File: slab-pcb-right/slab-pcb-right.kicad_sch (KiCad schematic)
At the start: 125 parts, among them J1 MagnetR, J2 MagnetL, J3 TRRS_R, J4 TRRS_L, J5 SSD1306, J6 Conn_01x06, Q1 MMBT3906, SW1 RotaryEncoder, U1 Seeeduino Xiao rp2040, U2 PCA9555PW, U3 PCA9555PW, U4 ADS1110, U5 SN74AHCT125PWR

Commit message: fix: inconsistent design
all modules now share the same design - with updated footprints to
support both choc+mx PCB mounting holes.
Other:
- company: (none) -> Edward Hesketh
- title: (none) -> The Slab Keyboard - Right Module
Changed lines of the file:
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@@
 	(generator_version "8.0")
 	(paper "A4")
+	(title_block
+		(title "The Slab Keyboard - Right Module")
+		(date "2024-10-16")
+		(company "Edward Hesketh")
+	)
 	(junction
 		(at 227.33 148.59)

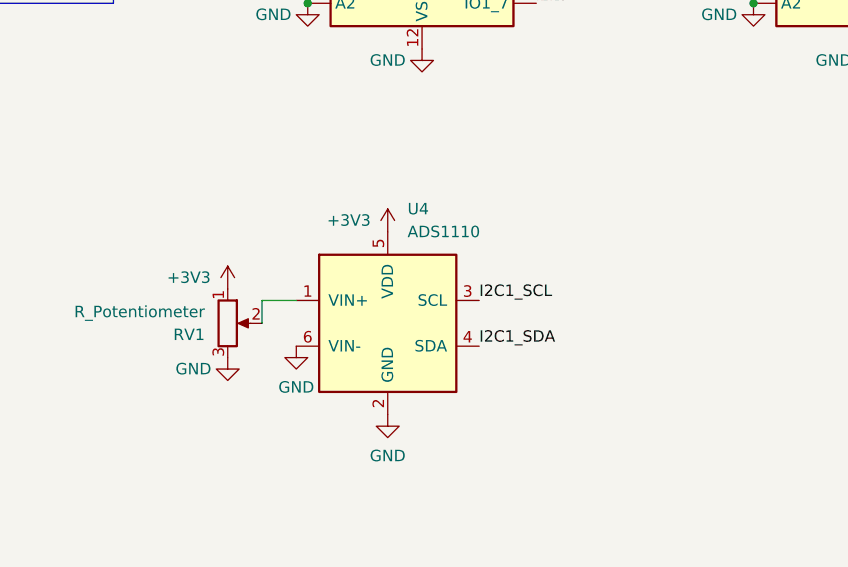
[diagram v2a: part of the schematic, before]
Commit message: fix: add voltage divider to potentiometer
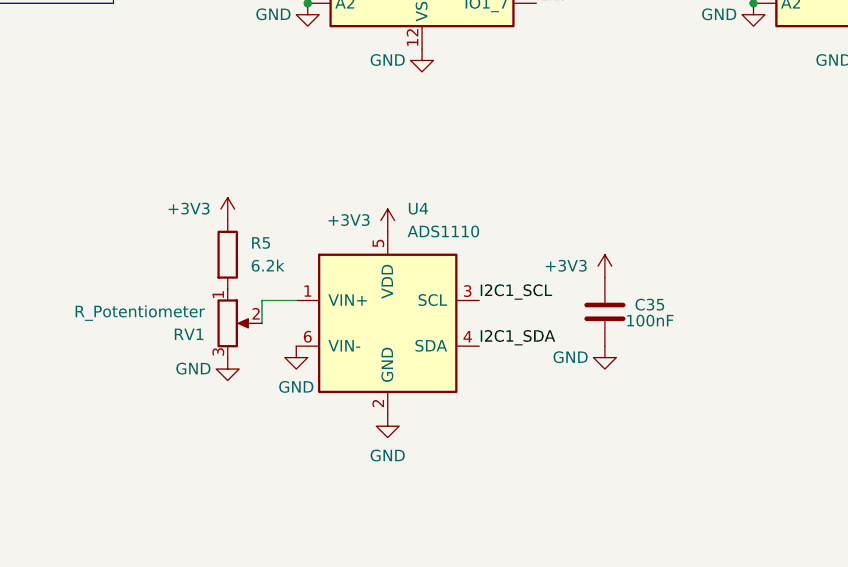
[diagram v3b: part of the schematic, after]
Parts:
- added C35: 100nF, Capacitor_SMD:C_0603_1608Metric_Pad1.08x0.95mm_HandSolder, symbol Device:C
- added R5: 6.2k, Resistor_SMD:R_0603_1608Metric_Pad0.98x0.95mm_HandSolder, symbol Device:R
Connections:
- net +3V3: now also C35.2, R5.1; no longer RV1.1
- net GND: now also C35.1
- new net: R5.2, RV1.1

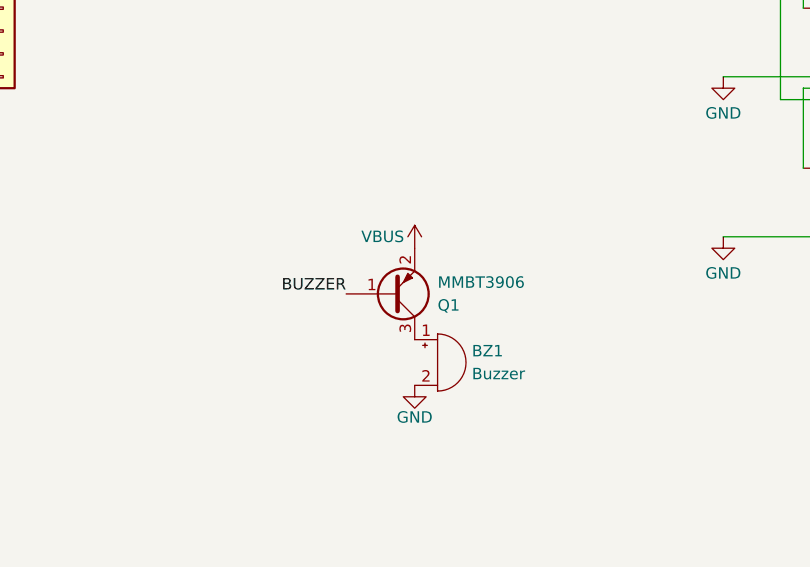
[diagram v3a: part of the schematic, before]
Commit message: feat: use slots instead of overlapped drill hits
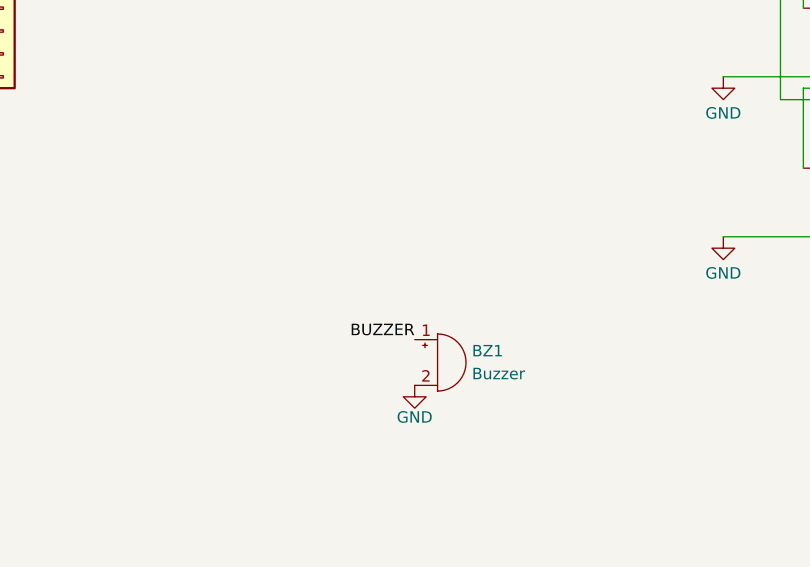
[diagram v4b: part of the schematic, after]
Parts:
- removed Q1: MMBT3906, Package_TO_SOT_SMD:SOT-23, symbol Transistor_BJT:MMBT3906
- BZ1: footprint Buzzer_Beeper:MagneticBuzzer_CUI_CMT-8504-100-SMT -> CustomFootprints:buzzer
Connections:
- net BUZZER: now also BZ1.1 (+)
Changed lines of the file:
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@@
 	)
 	(label "BUZZER"
-		(at 138.43 172.72 180)
+		(at 146.05 177.8 180)
 		(fields_autoplaced yes)
 		(effects
@@
 	)
 	(symbol
-		(lib_id "power:VBUS")
-		(at 146.05 167.64 0)
-		(unit 1)
-		(exclude_from_sim no)
-		(in_bom yes)
-		(on_board yes)
-		(dnp no)
-		(property "Reference" "#PWR039"
-			(at 146.05 171.45 0)
-			(effects
-				(font
-					(size 1.27 1.27)
-				)
-				(hide yes)
-			)
-		)
-		(property "Value" "VBUS"
-			(at 142.494 166.37 0)
-			(effects
-				(font
-					(size 1.27 1.27)
-				)
-			)
-		)
-		(property "Footprint" ""
-			(at 146.05 167.64 0)
-			(effects
-				(font
-					(size 1.27 1.27)
-				)
-				(hide yes)
-			)
-		)
-		(property "Datasheet" ""
-			(at 146.05 167.64 0)
-			(effects
-				(font
-					(size 1.27 1.27)
-				)
-				(hide yes)
-			)
-		)
-		(property "Description" "Power symbol creates a global label with name \"VBUS\""
-			(at 146.05 167.64 0)
-			(effects
-				(font
-					(size 1.27 1.27)
-				)
-				(hide yes)
-			)
-		)
-		(pin "1"
-		)
-		(instances
-			(project "slab-pcb-right"
-				(path "/2d36872c-cd86-4c0b-a812-2eca2fd821a3"
-					(reference "#PWR039")
-					(unit 1)
-				)
-			)
-		)
-	)
-	(symbol
 		(lib_id "Connector_Generic:Conn_01x04")
 		(at 55.88 133.35 180)
@@
 	)
 	(symbol
-		(lib_id "Transistor_BJT:MMBT3906")
-		(at 143.51 172.72 0)
-		(mirror x)
-		(unit 1)
-		(exclude_from_sim no)
-		(in_bom yes)
-		(on_board yes)
-		(dnp no)
-		(property "Reference" "Q1"
-			(at 148.59 173.9901 0)
-			(effects
-				(font
-					(size 1.27 1.27)
-				)
-				(justify left)
-			)
-		)
-		(property "Value" "MMBT3906"
-			(at 148.59 171.4501 0)
-			(effects
-				(font
-					(size 1.27 1.27)
-				)
-				(justify left)
-			)
-		)
-		(property "Footprint" "Package_TO_SOT_SMD:SOT-23"
-			(at 148.59 170.815 0)
-			(effects
-				(font
-					(size 1.27 1.27)
-					(italic yes)
-				)
-				(justify left)
-				(hide yes)
-			)
-		)
-		(property "Datasheet" "https://www.onsemi.com/pdf/datasheet/pzt3906-d.pdf"
-			(at 143.51 172.72 0)
-			(effects
-				(font
-					(size 1.27 1.27)
-				)
-				(justify left)
-				(hide yes)
-			)
-		)
-		(property "Description" "-0.2A Ic, -40V Vce, Small Signal PNP Transistor, SOT-23"
-			(at 143.51 172.72 0)
-			(effects
-				(font
-					(size 1.27 1.27)
-				)
-				(hide yes)
-			)
-		)
-		(pin "1"
-		)
-		(pin "3"
-		)
-		(pin "2"
-		)
-		(instances
-			(project "slab-pcb-right"
-				(path "/2d36872c-cd86-4c0b-a812-2eca2fd821a3"
-					(reference "Q1")
-					(unit 1)
-				)
-			)
-		)
-	)
-	(symbol
 		(lib_id "power:GND")
 		(at 180.34 113.03 0)
@@
 			)
 		)
-		(property "Footprint" "Buzzer_Beeper:MagneticBuzzer_CUI_CMT-8504-100-SMT"
+		(property "Footprint" "CustomFootprints:buzzer"
 			(at 147.955 177.8 90)
 			(effects

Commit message: feat: start on v4, updated: right-hand schematic
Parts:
- removed C1, C10, C11, C12, C13, C14, C15, C16, C17, C18, C19, C2, C20, C21, C22, C23, C24, C25, C26, C27, C28, C29, C3, C30, C4, C5, C6, C7, C8, C9: 100nF, Capacitor_SMD:C_0603_1608Metric_Pad1.08x0.95mm_HandSolder, symbol Device:C
- removed J6: Conn_01x06, Connector_PinHeader_2.54mm:PinHeader_1x06_P2.54mm_Vertical, symbol Connector_Generic:Conn_01x06
- removed LED1, LED10, LED11, LED12, LED13, LED14, LED15, LED16, LED17, LED18, LED19, LED2, LED20, LED21, LED22, LED23, LED24, LED25, LED26, LED27, LED28, LED29, LED3, LED30, LED4, LED5, LED6, LED7, LED8, LED9: MX_SK6812MINI-E, CustomFootprints:LED_MX_6028R-ROT_Custom, symbol PCM_marbastlib-mx:MX_SK6812MINI-E
- removed TP1: NPIXEL_SHIFT, TestPoint:TestPoint_Pad_1.0x1.0mm, symbol Connector:TestPoint
- removed TP2: NPIXEL_IN, TestPoint:TestPoint_Pad_1.0x1.0mm, symbol Connector:TestPoint
- added C36: 100nF, Capacitor_SMD:C_0603_1608Metric_Pad1.08x0.95mm_HandSolder, symbol Device:C
- added R10, R7, R8, R9: 2.2k, Resistor_SMD:R_0603_1608Metric_Pad0.98x0.95mm_HandSolder, symbol Device:R
- added R6: 10k, Resistor_SMD:R_0603_1608Metric_Pad0.98x0.95mm_HandSolder, symbol Device:R
- added U6: TCA4307DGKR, SOIC8_DGK_TEX, symbol CustomSymbols:TCA4307DGKR
- J1: value MagnetR -> Conn_01x04; footprint CustomFootprints:5358_mag_connector_1x4_pads -> (none)
- J2: value MagnetL -> Conn_01x04; footprint CustomFootprints:5358_mag_connector_1x4_pins -> (none)
- RV1: value R_Potentiometer -> Slider
- renumbered J4 to J3, J3 to J4
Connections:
- net UART0_RX is gone; now on net SHIFTER_INPUT: U1.14 (P1)
- net +3V3: now also C32.2, C33.2, C34.2, U5.14 (VCC), C36.2, R10.2, R6.1, R7.1, R8.1, R9.2, U6.1 (EN), U6.8 (VCC); no longer C32.1, C33.1
- net BUZZER: now also U1.11 (P3); no longer U1.13 (P2)
- net EXPANDER1_INT: now also U1.13 (P2); no longer U3.13 (IO1_0)
- net EXPANDER2_INT: now also U1.12 (P4); no longer U1.11 (P3)
- net GND: now also C32.1, C33.1, J1.3 (Pin_3), J2.3 (Pin_3), C36.1, U6.4 (GND); no longer C32.2, C33.2, J1.1 (Pin_1), J2.1 (Pin_1)
- net I2C0_SCL: now also J5.3 (Pin_3), R1.2, U2.22 (SCL), U3.22 (SCL), U4.3 (SCL); no longer J1.2 (Pin_2), J4.R1
- net I2C0_SDA: now also J5.4 (Pin_4), R2.2, U2.23 (SDA), U3.23 (SDA), U4.4 (SDA); no longer J1.3 (Pin_3), J4.R2
- net I2C1_SCL: now also R7.2, U6.2 (SCLOUT); no longer J2.2 (Pin_2), J3.R1, J5.3 (Pin_3), R2.2, U2.22 (SCL), U3.22 (SCL), U4.3 (SCL)
- net I2C1_SDA: now also R8.2, U6.7 (SDAOUT); no longer J2.3 (Pin_3), J3.R2, J5.4 (Pin_4), R1.2, U2.23 (SDA), U3.23 (SDA), U4.4 (SDA)
- net VBUS: no longer C34.2, U5.14 (VCC)
- net RGB LED Array/Output: now reaches LED31.3 (DIN)
- net ENCODER_A renamed ROT_A
- net ENCODER_B renamed ROT_B
- net KEY_PIXEL_INPUT renamed SHIFTER_OUTPUT
- net KEY_PIXEL_SHIFT_INPUT renamed SHIFTER_INPUT
- net SHIFTER_INPUT: no longer U1.12 (P4)
- net UART0_TX renamed I2C1_RDY
- net I2C1_RDY: now also R6.2, U6.5 (READY)
- new net I2C_BUS_SCL: J1.2 (Pin_2), J2.2 (Pin_2), J3.R2, J4.R2, R9.1, U6.3 (SCLIN)
- new net I2C_BUS_SDA: J1.1 (Pin_1), J2.1 (Pin_1), J3.R1, J4.R1, R10.1, U6.6 (SDAIN)
- no-connect marks 19 -> 18
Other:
- added sheet RGB LED Array (RGBLEDArray.kicad_sch)
- note added: "ADC and slider/potentiometer"
- note added: "Buzzer"
- note added: "I2C0 (to onboard peripherals)"
- note added: "I2C0 pullup resistors"
- note added: "I2C1 (to other keyboards)"
- note added: "Key switch array"
- note added: "Logic level changer and main LED array"
- note added: "OLED screen"
- note added: "Rotary encoder with LED"
- note removed: "Seeeduino Xiao RP2040"
- title: The Slab Keyboard - Right Module -> The Interchange Keyboard - Right Module
- moved on the sheet: BZ1, C32, H1, H2, H3, H4, H5, H6, H7, H8, H9, J3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

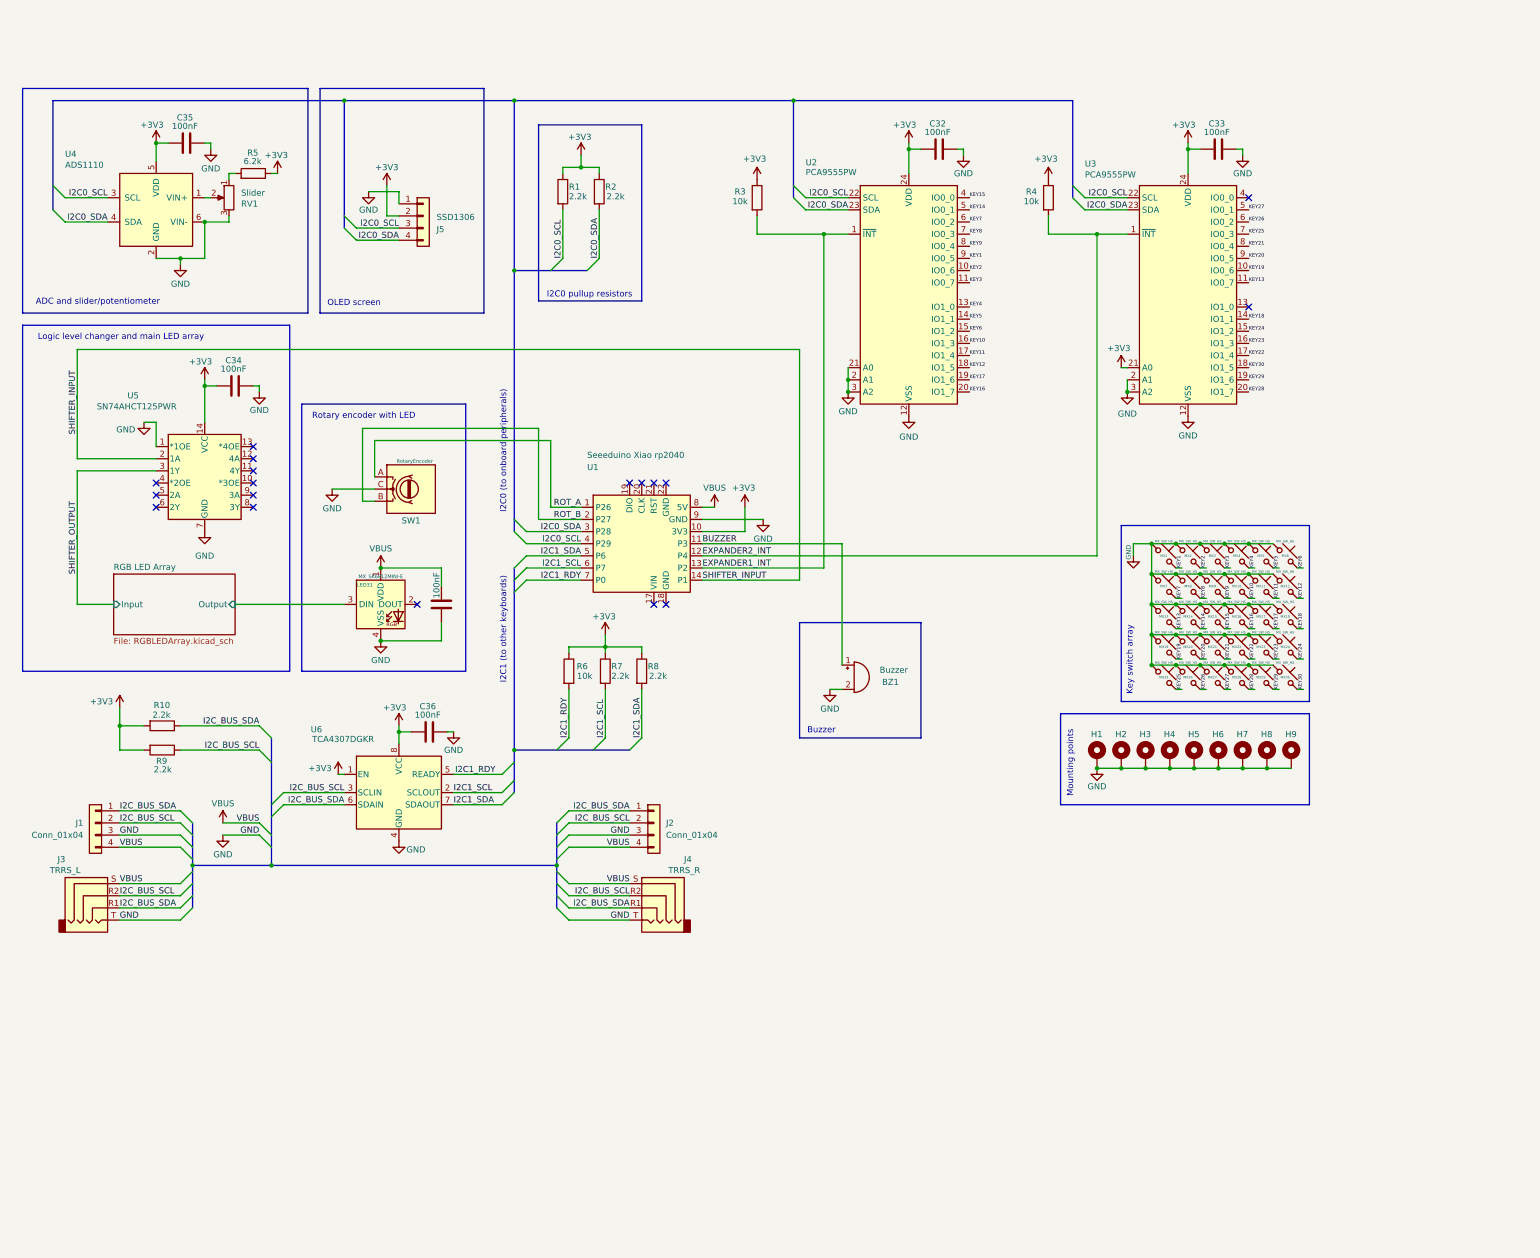
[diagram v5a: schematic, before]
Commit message: feat: route most of slab-pcb-right
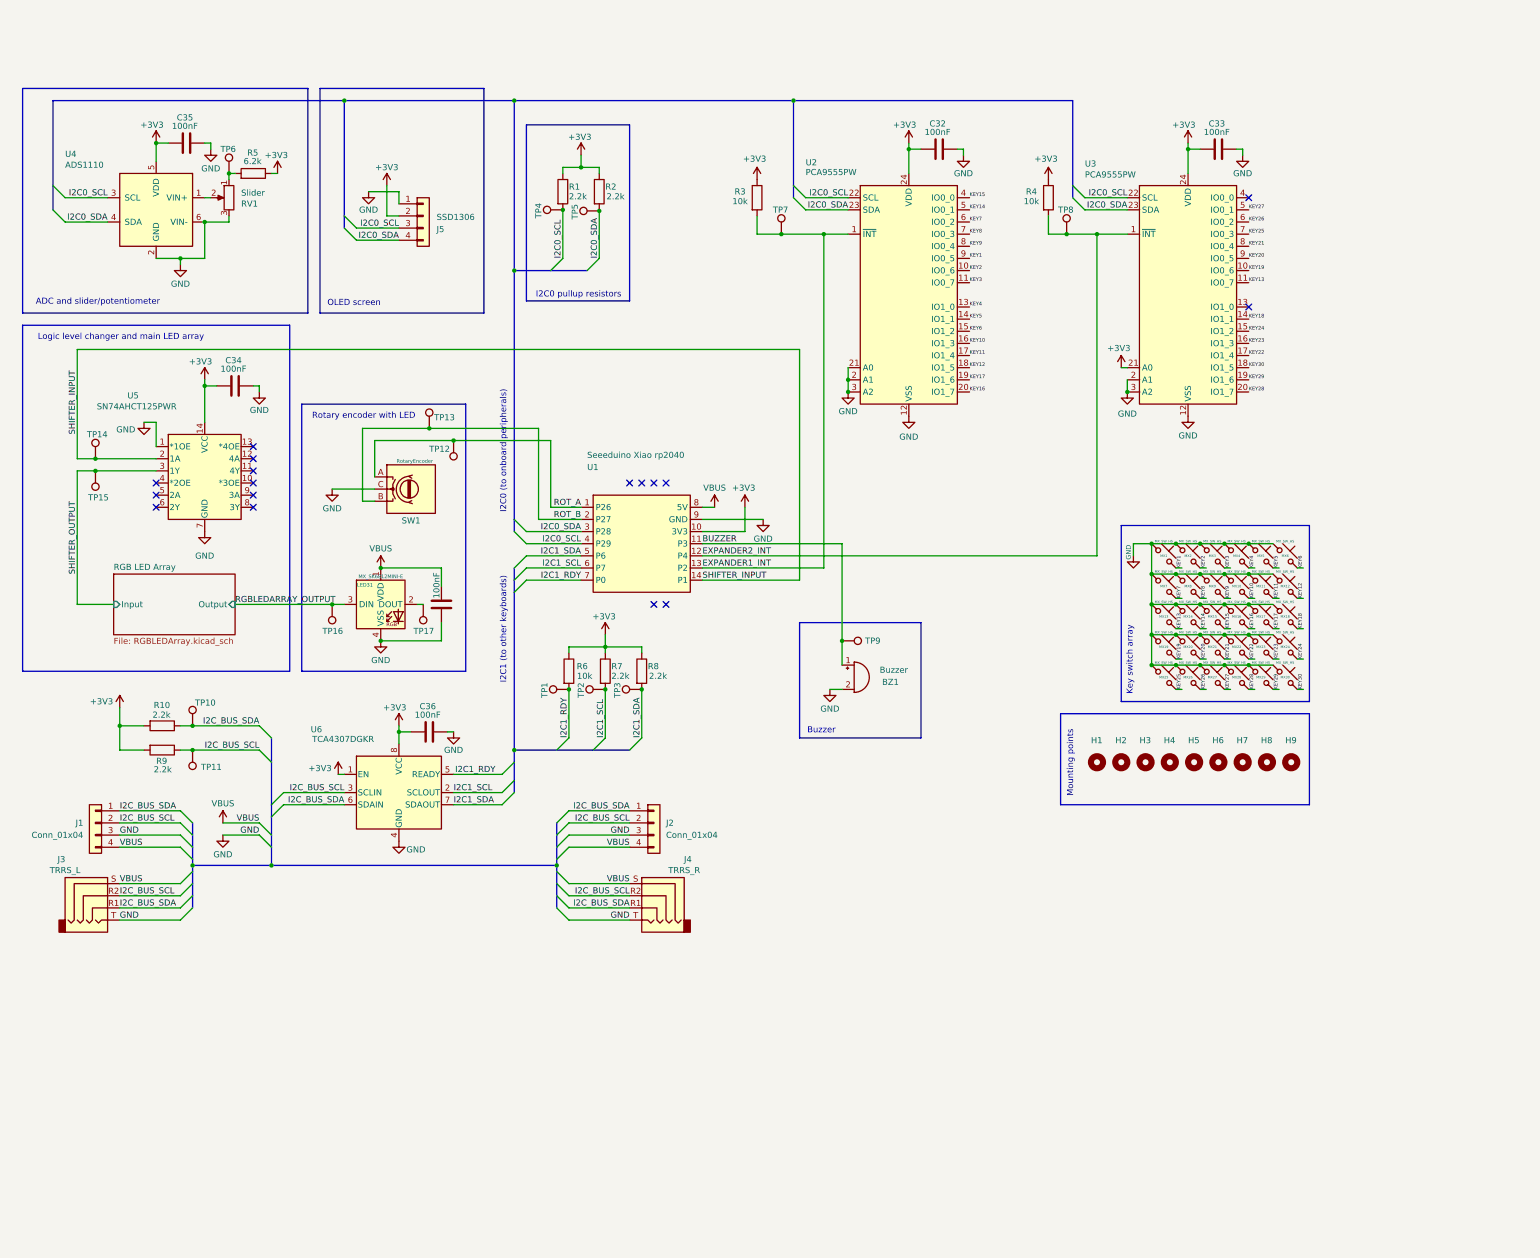
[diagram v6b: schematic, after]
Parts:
- added TP1, TP10, TP11, TP12, TP13, TP14, TP15, TP16, TP17, TP2, TP3, TP4, TP5, TP6, TP7, TP8, TP9: TestPoint, TestPoint:TestPoint_Pad_D1.5mm, symbol Connector:TestPoint
- H1, H2, H3, H4, H5, H6, H7, H8, H9: footprint MountingHole:MountingHole_3.2mm_M3_Pad_TopBottom -> MountingHole:MountingHole_3.2mm_M3; symbol Mechanical:MountingHole_Pad -> Mechanical:MountingHole; now left out of the parts list
- J1: footprint (none) -> CustomFootprints:MagneticSlot_Right
- J2: footprint (none) -> CustomFootprints:MagneticSlot_Left
- SW1: footprint Rotary_Encoder:RotaryEncoder_Alps_EC12E_Vertical_H20mm -> CustomFootprints:RotaryEncoder_Alps_EC12E_Vertical_H20mm_Custom
- U6: footprint SOIC8_DGK_TEX -> CustomFootprints:SOIC8_DGK_TEX
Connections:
- net BUZZER: now also TP9.1
- net EXPANDER1_INT: now also TP7.1
- net EXPANDER2_INT: now also TP8.1
- net GND: no longer H1.1, H2.1, H3.1, H4.1, H5.1, H6.1, H7.1, H8.1, H9.1
- net I2C0_SCL: now also TP4.1
- net I2C0_SDA: now also TP5.1
- net I2C1_RDY: now also TP1.1
- net I2C1_SCL: now also TP2.1
- net I2C1_SDA: now also TP3.1
- net I2C_BUS_SCL: now also TP11.1
- net I2C_BUS_SDA: now also TP10.1
- net ROT_A: now also TP12.1
- net ROT_B: now also TP13.1
- net SHIFTER_INPUT: now also TP14.1
- net SHIFTER_OUTPUT: now also TP15.1
- net at R5.2, RV1.1: now also TP6.1
- net at LED31.2 (DOUT): now also TP17.1
- net RGB LED Array/Output renamed RGBLEDARRAY_OUTPUT
- net RGBLEDARRAY_OUTPUT: now also TP16.1
- no-connect marks 18 -> 17
